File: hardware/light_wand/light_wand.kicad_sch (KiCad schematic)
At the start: 0 parts

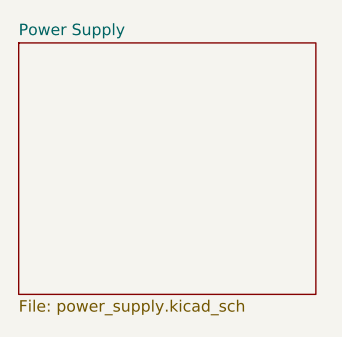
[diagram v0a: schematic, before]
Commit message: Added footprint for battery prot ic
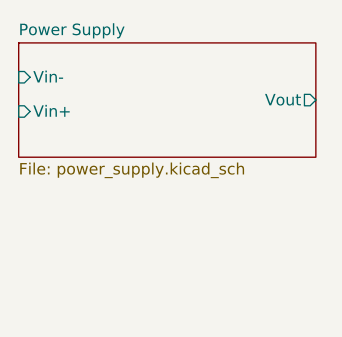
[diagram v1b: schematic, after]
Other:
- sheet Power Supply ports: added Vin+, Vin-, Vout; removed none
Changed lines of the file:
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@@
 (kicad_sch (version 20230121) (generator eeschema)
   (paper "A4")
-  (sheet (at 71.12 66.04) (size 33.02 27.94) (fields_autoplaced)
+  (sheet (at 71.12 66.04) (size 33.02 12.7) (fields_autoplaced)
     (stroke (width 0.1524) (type solid))
     (fill (color 0 0 0 0.0000))
@@
       (effects (font (size 1.27 1.27)) (justify left bottom))
     )
-    (property "Sheetfile" "power_supply.kicad_sch" (at 71.12 94.5646 0)
+    (property "Sheetfile" "power_supply.kicad_sch" (at 71.12 79.3246 0)
       (effects (font (size 1.27 1.27)) (justify left top))
     )
+    (pin "Vin-" input (at 71.12 69.85 180)
+      (effects (font (size 1.27 1.27)) (justify left))
+    )
+    (pin "Vin+" input (at 71.12 73.66 180)
+      (effects (font (size 1.27 1.27)) (justify left))
+    )
+    (pin "Vout" output (at 104.14 72.39 0)
+      (effects (font (size 1.27 1.27)) (justify right))
+    )
     (instances

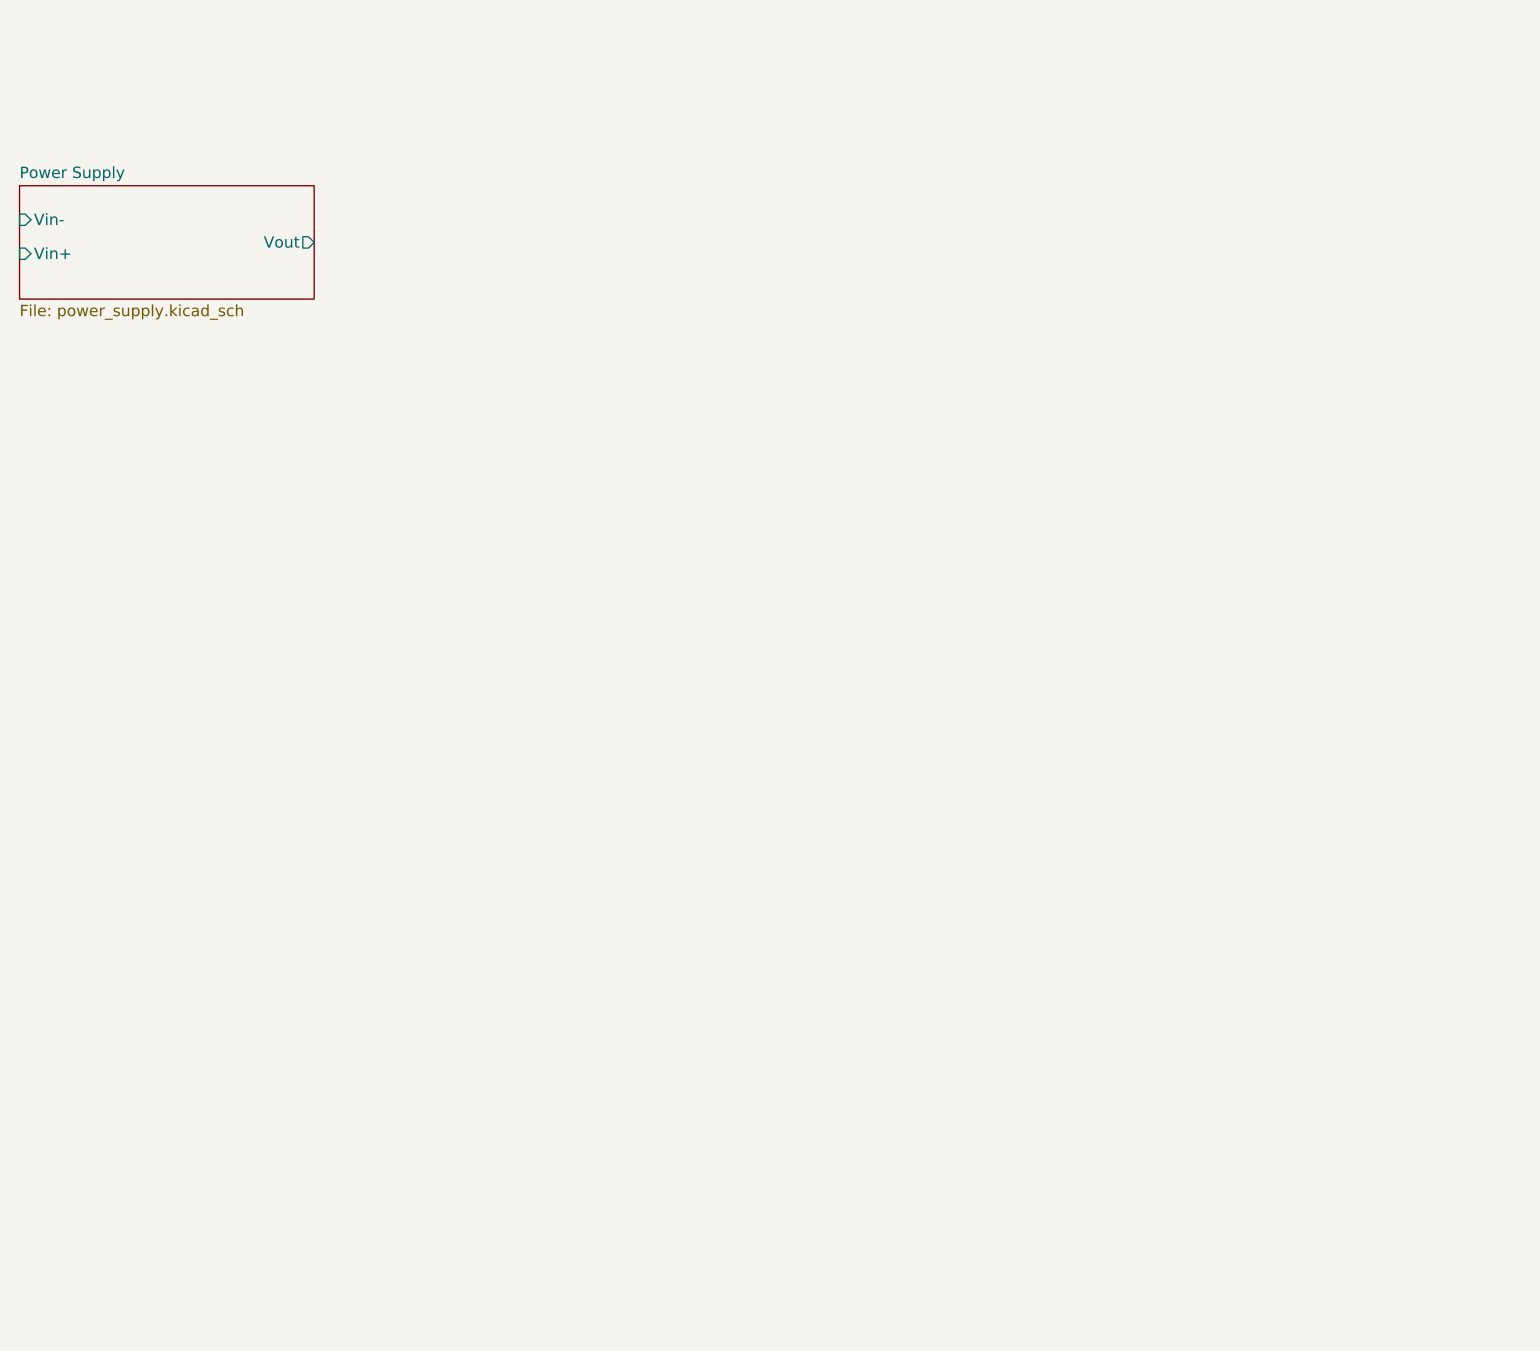
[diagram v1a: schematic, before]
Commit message: Added pico to the schematic
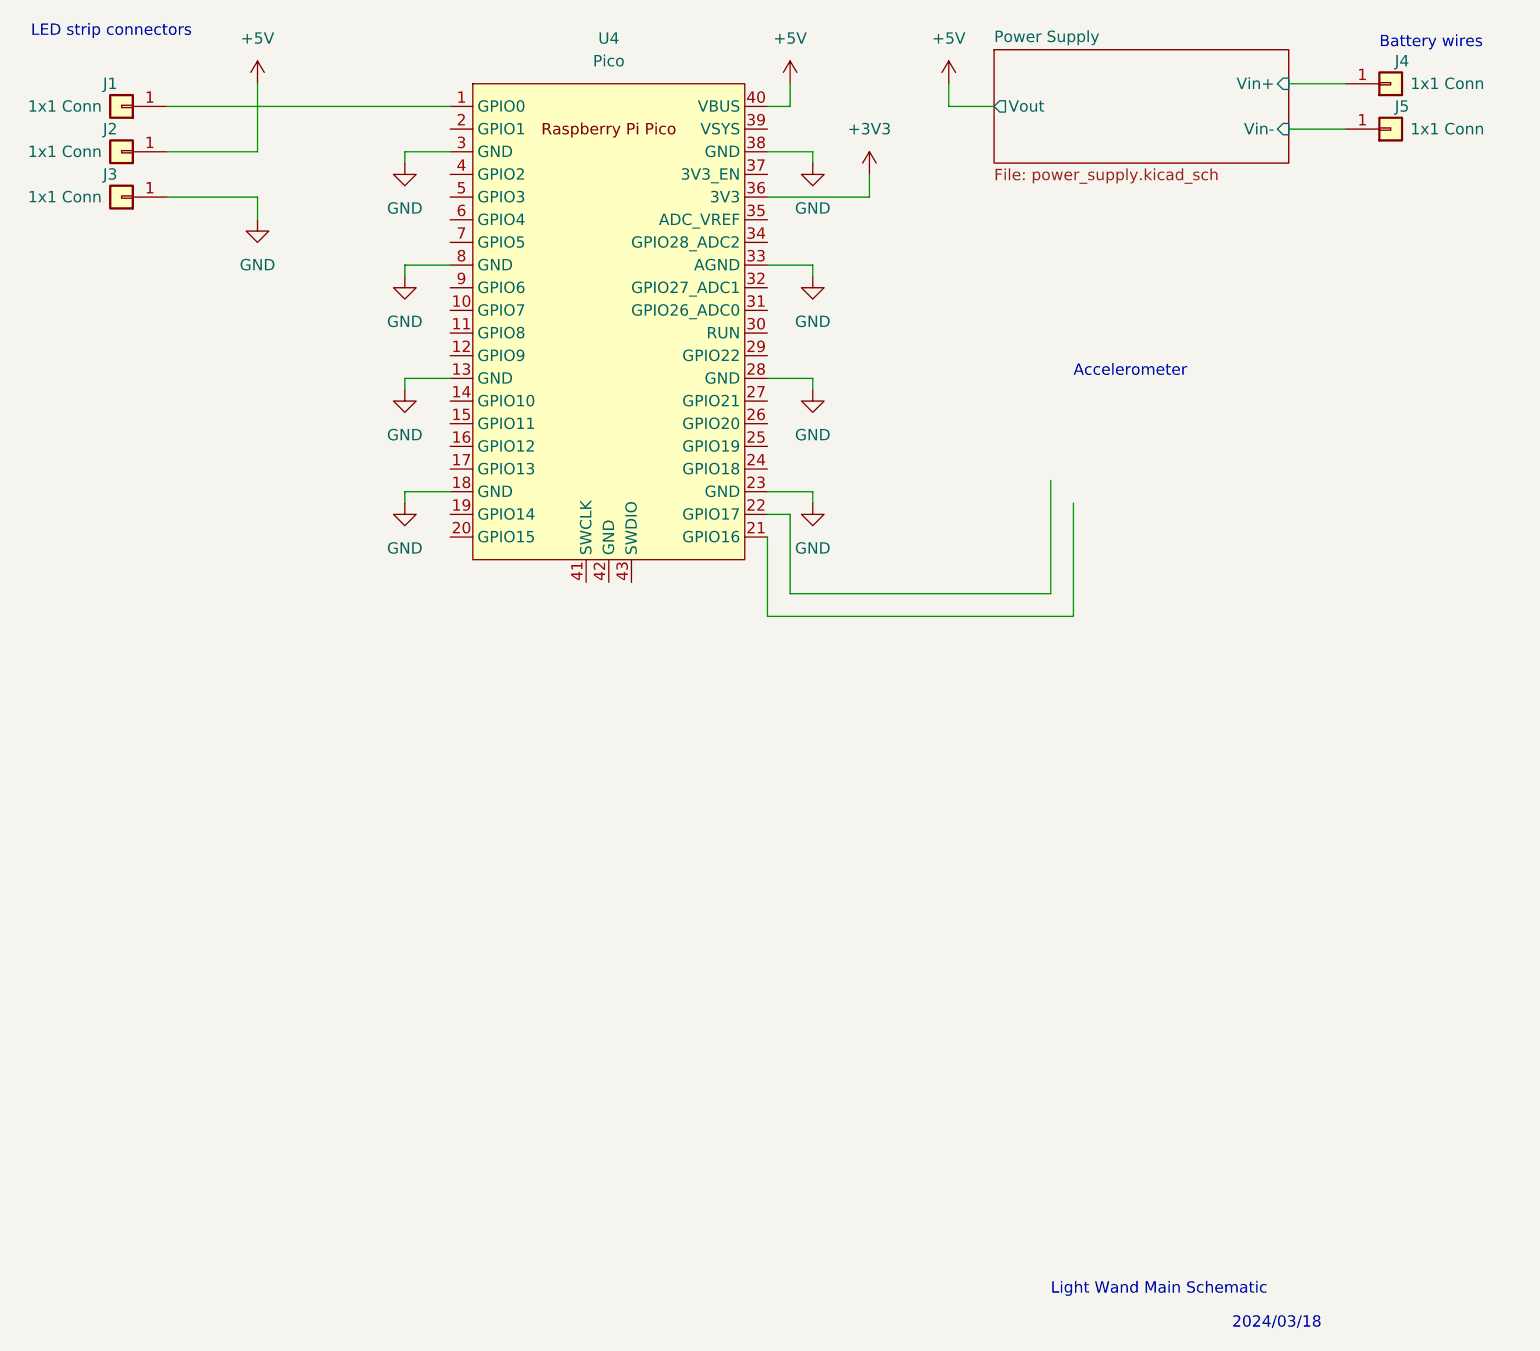
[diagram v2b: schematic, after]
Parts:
- added J1, J2, J3, J4, J5: 1x1 Conn, Connector_Wire:SolderWire-0.5sqmm_1x01_D0.9mm_OD2.1mm, symbol Connector_Generic:Conn_01x01
- added U4: Pico, MCU_RaspberryPi_and_Boards:RPi_Pico_SMD_TH, symbol MCU_RaspberryPi_and_Boards:Pico
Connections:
- net Power Supply/Vin+: now also J4.1 (Pin_1)
- net Power Supply/Vin-: now also J5.1 (Pin_1)
- new net: J1.1 (Pin_1), U4.1 (GPIO0)
- new net +3V3: U4.36 (3V3)
- new net +5V: J2.1 (Pin_1), U4.40 (VBUS)
- new net GND: J3.1 (Pin_1), U4.13 (GND), U4.18 (GND), U4.23 (GND), U4.28 (GND), U4.3 (GND), U4.33 (AGND), U4.38 (GND), U4.8 (GND)
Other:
- note added: "2024/03/18"
- note added: "Accelerometer"
- note added: "Battery wires"
- note added: "LED strip connectors"
- note added: "Light Wand Main Schematic"

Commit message: Completed circuit schematic
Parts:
- added U5: ~, light_wand_footprints:ADXL343_Breakout_ThruHole, symbol light_wand_library:ADXL343_Breakout
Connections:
- net +3V3: now also U5.5 (VIN)
- net GND: now also U4.42 (GND), U5.4 (GND), U5.7 (GND)
- net at U4.21 (GPIO16): now also U5.9 (SDA)
- net at U4.22 (GPIO17): now also U5.8 (SCL)
- no-connect marks 0 -> 34
